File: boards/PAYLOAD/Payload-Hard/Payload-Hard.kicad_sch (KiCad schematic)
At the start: 2 parts

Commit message: LL
LL
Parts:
- added J?: Conn_01x05_Female, symbol Connector:Conn_01x05_Female
- added P?: S3B-PH-SM4-TB, JST_S3B-PH-SM4-TB:JST_S3B-PH-SM4-TB, symbol S3B-PH-SM4-TB:S3B-PH-SM4-TB
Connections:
- net RED: now reaches A.19 (A0)
- net RED: now also J?.3 (Pin_3)
- net NOX: now reaches A.20 (A1)
- net NOX: now also J?.4 (Pin_4)
- net PRE: now reaches A.21 (A2)
- net PRE: now also J?.5 (Pin_5)
- net 5V: now reaches A.27 (+5V)
- net 5V: now also J?.1 (Pin_1), P?.2
- net GND: now reaches A.29 (GND)
- net GND: now also A.4 (GND), J?.2 (Pin_2), P?.1
- net SIG: now reaches A.5 (D2)
- net SIG: now also P?.3
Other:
- moved on the sheet: A, U?
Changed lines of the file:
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@@
 (kicad_sch (version 20211123) (generator eeschema)
   (paper "A4")
-  (symbol (lib_id "Sensor_Gas:3SP_SO2_20") (at 247.65 62.23 0) (unit 1)
-    (in_bom yes) (on_board yes) (fields_autoplaced)
-    (property "Reference" "U?" (id 0) (at 248.7295 59.69 0))
-    (property "Value" "3SP_SO2_20" (id 1) (at 248.7295 62.23 0))
-    (property "Footprint" "" (id 2) (at 247.65 62.23 0)
-      (effects (font (size 1.27 1.27)) hide)
-    )
-    (property "Datasheet" "" (id 3) (at 247.65 62.23 0)
+  (junction (at 163.83 87.63) (diameter 0) (color 0 0 0 0)
+  )
+  (wire (pts (xy 163.83 87.63) (xy 166.37 87.63))
+    (stroke (width 0) (type default) (color 0 0 0 0))
+  )
+  (wire (pts (xy 166.37 87.63) (xy 166.37 86.36))
+    (stroke (width 0) (type default) (color 0 0 0 0))
+  )
+  (wire (pts (xy 163.83 86.36) (xy 163.83 87.63))
+    (stroke (width 0) (type default) (color 0 0 0 0))
+  )
+  (wire (pts (xy 163.83 88.9) (xy 163.83 87.63))
+    (stroke (width 0) (type default) (color 0 0 0 0))
+  )
+  (hierarchical_label "5V" (shape input) (at 232.41 60.96 180)
+    (effects (font (size 1.27 1.27)) (justify right))
+  )
+  (hierarchical_label "NOX" (shape input) (at 176.53 63.5 0)
+    (effects (font (size 1.27 1.27)) (justify left))
+  )
+  (hierarchical_label "PRE" (shape input) (at 163.83 121.92 180)
+    (effects (font (size 1.27 1.27)) (justify right))
+  )
+  (hierarchical_label "SIG" (shape input) (at 151.13 50.8 180)
+    (effects (font (size 1.27 1.27)) (justify right))
+  )
+  (hierarchical_label "NOX" (shape input) (at 163.83 119.38 180)
+    (effects (font (size 1.27 1.27)) (justify right))
+  )
+  (hierarchical_label "RED" (shape input) (at 176.53 60.96 0)
+    (effects (font (size 1.27 1.27)) (justify left))
+  )
+  (hierarchical_label "RED" (shape input) (at 163.83 116.84 180)
+    (effects (font (size 1.27 1.27)) (justify right))
+  )
+  (hierarchical_label "PRE" (shape input) (at 176.53 66.04 0)
+    (effects (font (size 1.27 1.27)) (justify left))
+  )
+  (hierarchical_label "SIG" (shape input) (at 232.41 63.5 180)
+    (effects (font (size 1.27 1.27)) (justify right))
+  )
+  (hierarchical_label "5V" (shape input) (at 168.91 35.56 90)
+    (effects (font (size 1.27 1.27)) (justify left))
+  )
+  (hierarchical_label "5V" (shape input) (at 163.83 111.76 180)
+    (effects (font (size 1.27 1.27)) (justify right))
+  )
+  (symbol (lib_id "power:GND") (at 232.41 58.42 270) (unit 1)
+    (in_bom yes) (on_board yes) (fields_autoplaced)
+    (property "Reference" "#PWR?" (id 0) (at 226.06 58.42 0)
+      (effects (font (size 1.27 1.27)) hide)
+    )
+    (property "Value" "GND" (id 1) (at 228.6 58.4199 90)
+      (effects (font (size 1.27 1.27)) (justify right))
+    )
+    (property "Footprint" "" (id 2) (at 232.41 58.42 0)
+      (effects (font (size 1.27 1.27)) hide)
+    )
+    (property "Datasheet" "" (id 3) (at 232.41 58.42 0)
+      (effects (font (size 1.27 1.27)) hide)
+    )
+    (pin "1")
+  )
+  (symbol (lib_id "Sensor_Gas:3SP_SO2_20") (at 97.79 58.42 0) (unit 1)
+    (in_bom yes) (on_board yes) (fields_autoplaced)
+    (property "Reference" "U?" (id 0) (at 98.8695 55.88 0))
+    (property "Value" "3SP_SO2_20" (id 1) (at 98.8695 58.42 0))
+    (property "Footprint" "" (id 2) (at 97.79 58.42 0)
+      (effects (font (size 1.27 1.27)) hide)
+    )
+    (property "Datasheet" "" (id 3) (at 97.79 58.42 0)
       (effects (font (size 1.27 1.27)) hide)
     )
@@
     (pin "6")
   )
-  (symbol (lib_id "MCU_Module:Arduino_Nano_v3.x") (at 154.94 81.28 0) (unit 1)
-    (in_bom yes) (on_board yes) (fields_autoplaced)
-    (property "Reference" "A" (id 0) (at 159.4994 106.68 0)
-      (effects (font (size 1.27 1.27)) (justify left))
-    )
-    (property "Value" "Arduino_Nano_v3.x" (id 1) (at 159.4994 109.22 0)
-      (effects (font (size 1.27 1.27)) (justify left))
-    )
-    (property "Footprint" "Module:Arduino_Nano" (id 2) (at 154.94 81.28 0)
+  (symbol (lib_id "MCU_Module:Arduino_Nano_v3.x") (at 163.83 60.96 0) (unit 1)
+    (in_bom yes) (on_board yes) (fields_autoplaced)
+    (property "Reference" "A" (id 0) (at 168.3894 86.36 0)
+      (effects (font (size 1.27 1.27)) (justify left))
+    )
+    (property "Value" "Arduino_Nano_v3.x" (id 1) (at 168.3894 88.9 0)
+      (effects (font (size 1.27 1.27)) (justify left))
+    )
+    (property "Footprint" "Module:Arduino_Nano" (id 2) (at 163.83 60.96 0)
       (effects (font (size 1.27 1.27) italic) hide)
     )
-    (property "Datasheet" "http://www.mouser.com/pdfdocs/Gravitech_Arduino_Nano3_0.pdf" (id 3) (at 154.94 81.28 0)
+    (property "Datasheet" "http://www.mouser.com/pdfdocs/Gravitech_Arduino_Nano3_0.pdf" (id 3) (at 163.83 60.96 0)
       (effects (font (size 1.27 1.27)) hide)
     )
@@
     (pin "9")
   )
+  (symbol (lib_id "power:GND") (at 163.83 88.9 0) (unit 1)
+    (in_bom yes) (on_board yes) (fields_autoplaced)
+    (property "Reference" "#PWR?" (id 0) (at 163.83 95.25 0)
+      (effects (font (size 1.27 1.27)) hide)
+    )
+    (property "Value" "GND" (id 1) (at 163.83 93.98 0))
+    (property "Footprint" "" (id 2) (at 163.83 88.9 0)
+      (effects (font (size 1.27 1.27)) hide)
+    )
+    (property "Datasheet" "" (id 3) (at 163.83 88.9 0)
+      (effects (font (size 1.27 1.27)) hide)
+    )
+    (pin "1")
+  )
+  (symbol (lib_id "Connector:Conn_01x05_Female") (at 168.91 116.84 0) (unit 1)
+    (in_bom yes) (on_board yes) (fields_autoplaced)
+    (property "Reference" "J?" (id 0) (at 170.18 115.5699 0)
+      (effects (font (size 1.27 1.27)) (justify left))
+    )
+    (property "Value" "Conn_01x05_Female" (id 1) (at 170.18 118.1099 0)
+      (effects (font (size 1.27 1.27)) (justify left))
+    )
+    (property "Footprint" "" (id 2) (at 168.91 116.84 0)
+      (effects (font (size 1.27 1.27)) hide)
+    )
+    (property "Datasheet" "~" (id 3) (at 168.91 116.84 0)
+      (effects (font (size 1.27 1.27)) hide)
+    )
+    (pin "1")
+    (pin "2")
+    (pin "3")
+    (pin "4")
+    (pin "5")
+  )
+  (symbol (lib_id "S3B-PH-SM4-TB:S3B-PH-SM4-TB") (at 237.49 60.96 0) (unit 1)
+    (in_bom yes) (on_board yes) (fields_autoplaced)
+    (property "Reference" "P?" (id 0) (at 243.84 59.6899 0)
+      (effects (font (size 1.27 1.27)) (justify left))
+    )
+    (property "Value" "S3B-PH-SM4-TB" (id 1) (at 243.84 62.2299 0)
+      (effects (font (size 1.27 1.27)) (justify left))
+    )
+    (property "Footprint" "JST_S3B-PH-SM4-TB:JST_S3B-PH-SM4-TB" (id 2) (at 237.49 60.96 0)
+      (effects (font (size 1.27 1.27)) (justify bottom) hide)
+    )
+    (property "Datasheet" "" (id 3) (at 237.49 60.96 0)
+      (effects (font (size 1.27 1.27)) hide)
+    )
+    (property "MANUFACTURER" "JST" (id 4) (at 237.49 60.96 0)
+      (effects (font (size 1.27 1.27)) (justify bottom) hide)
+    )
+    (pin "1")
+    (pin "2")
+    (pin "3")
+  )
+  (symbol (lib_id "power:GND") (at 163.83 114.3 270) (unit 1)
+    (in_bom yes) (on_board yes)
+    (property "Reference" "#PWR?" (id 0) (at 157.48 114.3 0)
+      (effects (font (size 1.27 1.27)) hide)
+    )
+    (property "Value" "GND" (id 1) (at 160.02 114.3 90)
+      (effects (font (size 1.27 1.27)) (justify right))
+    )
+    (property "Footprint" "" (id 2) (at 163.83 114.3 0)
+      (effects (font (size 1.27 1.27)) hide)
+    )
+    (property "Datasheet" "" (id 3) (at 163.83 114.3 0)
+      (effects (font (size 1.27 1.27)) hide)
+    )
+    (pin "1")
+  )
   (sheet_instances
     (path "/" (page "1"))
   )
   (symbol_instances
+    (path "/196bc3c3-e5ff-458f-8b12-ac7c3d955c8b"
+      (reference "#PWR?") (unit 1) (value "GND") (footprint "")
+    )
+    (path "/b797a9a5-ff96-4bc7-9f7a-f6d641e801e6"
+      (reference "#PWR?") (unit 1) (value "GND") (footprint "")
+    )
+    (path "/e1403e9c-d28d-4e8c-a906-1d3b4236ad77"
+      (reference "#PWR?") (unit 1) (value "GND") (footprint "")
+    )
     (path "/a91a09ae-7da8-46f5-893f-cfe40ca8737a"
       (reference "A") (unit 1) (value "Arduino_Nano_v3.x") (footprint "Module:Arduino_Nano")
     )
+    (path "/bc1d1c15-132d-4a77-beb4-5670c0f8e9de"
+      (reference "J?") (unit 1) (value "Conn_01x05_Female") (footprint "")
+    )
+    (path "/ca60eda0-66cc-44d6-94f2-b6dbdfb5e6f4"
+      (reference "P?") (unit 1) (value "S3B-PH-SM4-TB") (footprint "JST_S3B-PH-SM4-TB:JST_S3B-PH-SM4-TB")
+    )
     (path "/325b982e-7665-4281-8762-9f7b5f3809a1"

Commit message: A Lot
A Lot
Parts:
- added C? (x2): 0.1uF, symbol Device:C
- added C?: 100 nF, Capacitor_SMD:C_0805_2012Metric, symbol D24V50F5:C
- added J?: Micro_SD_Card, Connector_Card:microSD_HC_Hirose_DM3AT-SF-PEJM5, symbol Connector:Micro_SD_Card
- added R? (x5): R_US, symbol Device:R_US
- added R? (x2): 10k, Resistor_SMD:R_0805_2012Metric, symbol D24V50F5:R_US
- added R?: 150 Ohm, symbol Device:R_US
- added U?: Opamp_Dual, symbol Device:Opamp_Dual
- added U?: OPAMP, symbol pspice:OPAMP
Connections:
- net GND: now also C?.1, J?.6 (VSS), J?.9 (SHIELD), R?.2, R?.2, U?.5 (V-)
- net at U?.1 (Working): now also U?.6 (Working)
- net Reference: now reaches U?.4 (Reference)
- net Reference: now also C?.2, U?.2 (-)
- net Counter: now reaches U?.5 (Counter)
- net Counter: now also C?.1, U?.3
- net 3V3: now reaches A.17 (3V3)
- net 3V3: now also C?.2, J?.4 (VDD), R?.1, R?.1, R?.1, R?.1, U?.4 (V+)
- net SO2_Out: now reaches A.22 (A3)
- net SPI_SDCARD_CS: now reaches A.6 (D3)
- net SPI_SDCARD_CS: now also J?.2 (DAT3/CD)
- net SPI_SDCARD_MOSI: now reaches A.7 (D4)
- net SPI_SDCARD_MOSI: now also J?.3 (CMD)
- net SPI_SDCARD_SCK: now reaches A.8 (D5)
- net SPI_SDCARD_SCK: now also J?.5 (CLK)
- net SPI_SDCARD_MISO: now reaches A.9 (D6)
- net SPI_SDCARD_MISO: now also J?.7 (DAT0)
- new net: C?.2, R?.2, U?.1
- new net: C?.1, R?.1, R?.2, U?.2 (-)
- new net: R?.1, R?.2, U?.3 (+)
- new net: R?.1, R?.2, U?.1 (+)
- new net: J?.1 (DAT2), R?.2
- new net: J?.8 (DAT1), R?.2
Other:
- note added: "Arduino V3"
- note added: "CO Sensor"
- note added: "Dust Sensor"
- note added: "Micro_SD_Card_Reader"
- note added: "SO2 Sensor"
- title: (none) -> My Dick is Hard 4 U
- moved on the sheet: U?

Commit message: Schematic Finished
Look it over
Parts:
- added J103: Conn_01x07_Male, symbol Connector:Conn_01x07_Male
- gave numbers to parts that had none: 17
- renumbered A to A101
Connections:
- net 3V3: now also J103.6 (Pin_6)
- net 5V: now also J103.7 (Pin_7)
- net SO2_Out: now also C103.2, R108.2, U103.1
- net SPI_SDCARD_CS: now also J103.2 (Pin_2)
- net SPI_SDCARD_MISO: now also J103.5 (Pin_5)
- net SPI_SDCARD_MOSI: now also J103.3 (Pin_3)
- net SPI_SDCARD_SCK: now also J103.4 (Pin_4)
- net SIG renamed Dust_SIG
- net Dust_SIG: now also J103.1 (Pin_1)
- no-connect marks 0 -> 19
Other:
- note added: "Test Pins"

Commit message: Added SO2 Footprint
See above
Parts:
- C102, C103, R101, R102, R105, R106, R107, R108: footprint (none) -> Resistor_SMD:R_0805_2012Metric
- J102, J103: footprint (none) -> Connector_PinSocket_2.54mm:PinSocket_1x07_P2.54mm_Vertical
- U102: footprint (none) -> Sensor:3SP_SO2_20
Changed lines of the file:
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@@
     (property "Reference" "R101" (id 0) (at 36.195 149.86 90))
     (property "Value" "R_US" (id 1) (at 36.195 152.4 90))
-    (property "Footprint" "" (id 2) (at 36.449 155.194 90)
+    (property "Footprint" "Resistor_SMD:R_0805_2012Metric" (id 2) (at 36.449 155.194 90)
       (effects (font (size 1.27 1.27)) hide)
     )
@@
     (property "Reference" "R108" (id 0) (at 147.32 135.255 90))
     (property "Value" "R_US" (id 1) (at 154.94 135.255 90))
-    (property "Footprint" "" (id 2) (at 150.749 136.779 90)
+    (property "Footprint" "Resistor_SMD:R_0805_2012Metric" (id 2) (at 150.749 136.779 90)
       (effects (font (size 1.27 1.27)) hide)
     )
@@
     (property "Reference" "U102" (id 0) (at 105.9815 150.114 0))
     (property "Value" "3SP_SO2_20" (id 1) (at 105.9815 152.654 0))
-    (property "Footprint" "" (id 2) (at 104.902 152.654 0)
+    (property "Footprint" "Sensor:3SP_SO2_20" (id 2) (at 104.902 152.654 0)
       (effects (font (size 1.27 1.27)) hide)
     )
@@
       (effects (font (size 1.27 1.27)) (justify left))
     )
-    (property "Footprint" "" (id 2) (at 81.6102 151.765 0)
+    (property "Footprint" "Resistor_SMD:R_0805_2012Metric" (id 2) (at 81.6102 151.765 0)
       (effects (font (size 1.27 1.27)) hide)
     )
@@
     (property "Reference" "J103" (id 0) (at 237.617 90.17 0))
     (property "Value" "Conn_01x07_Male" (id 1) (at 237.617 92.71 0))
-    (property "Footprint" "" (id 2) (at 236.982 102.616 0)
+    (property "Footprint" "Connector_PinSocket_2.54mm:PinSocket_1x07_P2.54mm_Vertical" (id 2) (at 236.982 102.616 0)
       (effects (font (size 1.27 1.27)) hide)
     )
@@
     (property "Reference" "R106" (id 0) (at 133.985 142.24 90))
     (property "Value" "150 Ohm" (id 1) (at 133.985 147.32 90))
-    (property "Footprint" "" (id 2) (at 134.239 143.764 90)
+    (property "Footprint" "Resistor_SMD:R_0805_2012Metric" (id 2) (at 134.239 143.764 90)
       (effects (font (size 1.27 1.27)) hide)
     )
@@
       (effects (font (size 1.27 1.27)) (justify left))
     )
-    (property "Footprint" "" (id 2) (at 44.831 164.084 90)
+    (property "Footprint" "Resistor_SMD:R_0805_2012Metric" (id 2) (at 44.831 164.084 90)
       (effects (font (size 1.27 1.27)) hide)
     )
@@
       (effects (font (size 1.27 1.27)) (justify left))
     )
-    (property "Footprint" "" (id 2) (at 137.541 164.084 90)
+    (property "Footprint" "Resistor_SMD:R_0805_2012Metric" (id 2) (at 137.541 164.084 90)
       (effects (font (size 1.27 1.27)) hide)
     )
@@
     (property "Reference" "C103" (id 0) (at 147.955 142.24 90))
     (property "Value" "0.1uF" (id 1) (at 153.035 142.24 90))
-    (property "Footprint" "" (id 2) (at 154.305 143.8148 0)
+    (property "Footprint" "Resistor_SMD:R_0805_2012Metric" (id 2) (at 154.305 143.8148 0)
       (effects (font (size 1.27 1.27)) hide)
     )
@@
       (effects (font (size 1.27 1.27)) (justify left))
     )
-    (property "Footprint" "" (id 2) (at 168.91 116.84 0)
+    (property "Footprint" "Connector_PinSocket_2.54mm:PinSocket_1x07_P2.54mm_Vertical" (id 2) (at 168.91 116.84 0)
       (effects (font (size 1.27 1.27)) hide)
     )
@@
     (property "Reference" "R105" (id 0) (at 129.54 149.225 90))
     (property "Value" "R_US" (id 1) (at 129.54 154.305 90))
-    (property "Footprint" "" (id 2) (at 129.794 150.749 90)
+    (property "Footprint" "Resistor_SMD:R_0805_2012Metric" (id 2) (at 129.794 150.749 90)
       (effects (font (size 1.27 1.27)) hide)
     )
@@
     )
     (path "/3785a743-d774-4bea-ab16-8819dd3926f7"
-      (reference "C102") (unit 1) (value "0.1uF") (footprint "")
+      (reference "C102") (unit 1) (value "0.1uF") (footprint "Resistor_SMD:R_0805_2012Metric")
     )
     (path "/ba5b7d76-cf69-4698-9e2c-a9beaffc4bab"
-      (reference "C103") (unit 1) (value "0.1uF") (footprint "")
+      (reference "C103") (unit 1) (value "0.1uF") (footprint "Resistor_SMD:R_0805_2012Metric")
     )
     (path "/aad04261-e627-4861-b410-22b45606c5aa"
@@
     )
     (path "/bc1d1c15-132d-4a77-beb4-5670c0f8e9de"
-      (reference "J102") (unit 1) (value "Conn_01x05_Female") (footprint "")
+      (reference "J102") (unit 1) (value "Conn_01x05_Female") (footprint "Connector_PinSocket_2.54mm:PinSocket_1x07_P2.54mm_Vertical")
     )
     (path "/3fd118c7-9e7a-4c5d-a6a1-1ac96967b8b9"
-      (reference "J103") (unit 1) (value "Conn_01x07_Male") (footprint "")
+      (reference "J103") (unit 1) (value "Conn_01x07_Male") (footprint "Connector_PinSocket_2.54mm:PinSocket_1x07_P2.54mm_Vertical")
     )
     (path "/ca60eda0-66cc-44d6-94f2-b6dbdfb5e6f4"
@@
     )
     (path "/193d0700-60b7-4689-978d-a547e5d96307"
-      (reference "R101") (unit 1) (value "R_US") (footprint "")
+      (reference "R101") (unit 1) (value "R_US") (footprint "Resistor_SMD:R_0805_2012Metric")
     )
     (path "/9250d66a-a257-4378-b8f5-d3bb8f4fd8a7"
-      (reference "R102") (unit 1) (value "R_US") (footprint "")
+      (reference "R102") (unit 1) (value "R_US") (footprint "Resistor_SMD:R_0805_2012Metric")
     )
     (path "/7d9c8643-fe41-4ec3-bc8b-c5590f819487"
@@
     )
     (path "/c6a3b258-40e8-4601-9207-4a2518b36ffa"
-      (reference "R105") (unit 1) (value "R_US") (footprint "")
+      (reference "R105") (unit 1) (value "R_US") (footprint "Resistor_SMD:R_0805_2012Metric")
     )
     (path "/85f2d637-1216-4a5c-bbc8-0ce2cc90f2ed"
-      (reference "R106") (unit 1) (value "150 Ohm") (footprint "")
+      (reference "R106") (unit 1) (value "150 Ohm") (footprint "Resistor_SMD:R_0805_2012Metric")
     )
     (path "/b9e4634e-89c4-4a0f-b5cd-8f409b547f37"
-      (reference "R107") (unit 1) (value "R_US") (footprint "")
+      (reference "R107") (unit 1) (value "R_US") (footprint "Resistor_SMD:R_0805_2012Metric")
     )
     (path "/2a4fc409-e0b4-4d3d-9f51-9b6d5ca0ec54"
-      (reference "R108") (unit 1) (value "R_US") (footprint "")
+      (reference "R108") (unit 1) (value "R_US") (footprint "Resistor_SMD:R_0805_2012Metric")
     )
     (path "/dea62b05-f679-4afa-8d03-361e4a7b827c"
@@
     )
     (path "/325b982e-7665-4281-8762-9f7b5f3809a1"
-      (reference "U102") (unit 1) (value "3SP_SO2_20") (footprint "")
+      (reference "U102") (unit 1) (value "3SP_SO2_20") (footprint "Sensor:3SP_SO2_20")
     )
     (path "/03c3a716-241d-43da-b0af-01f857d80378"

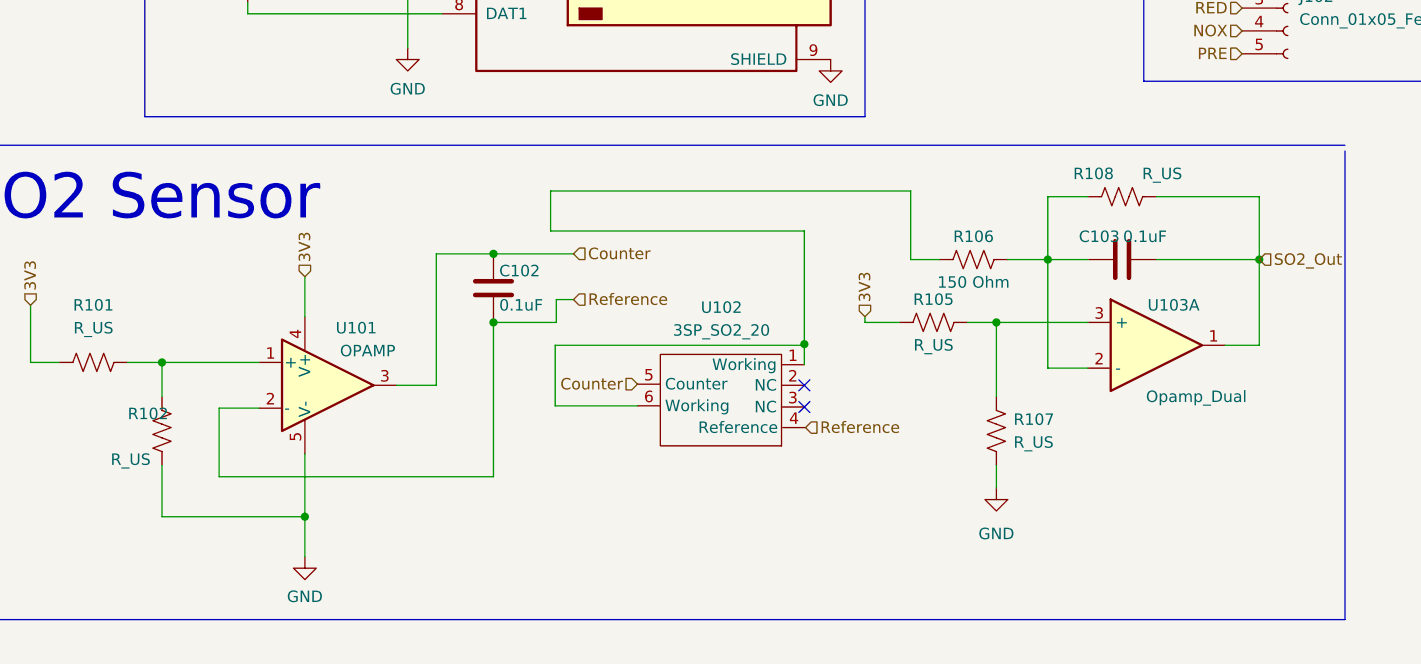
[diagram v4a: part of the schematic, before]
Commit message: Fixed Op Amp Circuitry
Fixed Op Amp Circuitry
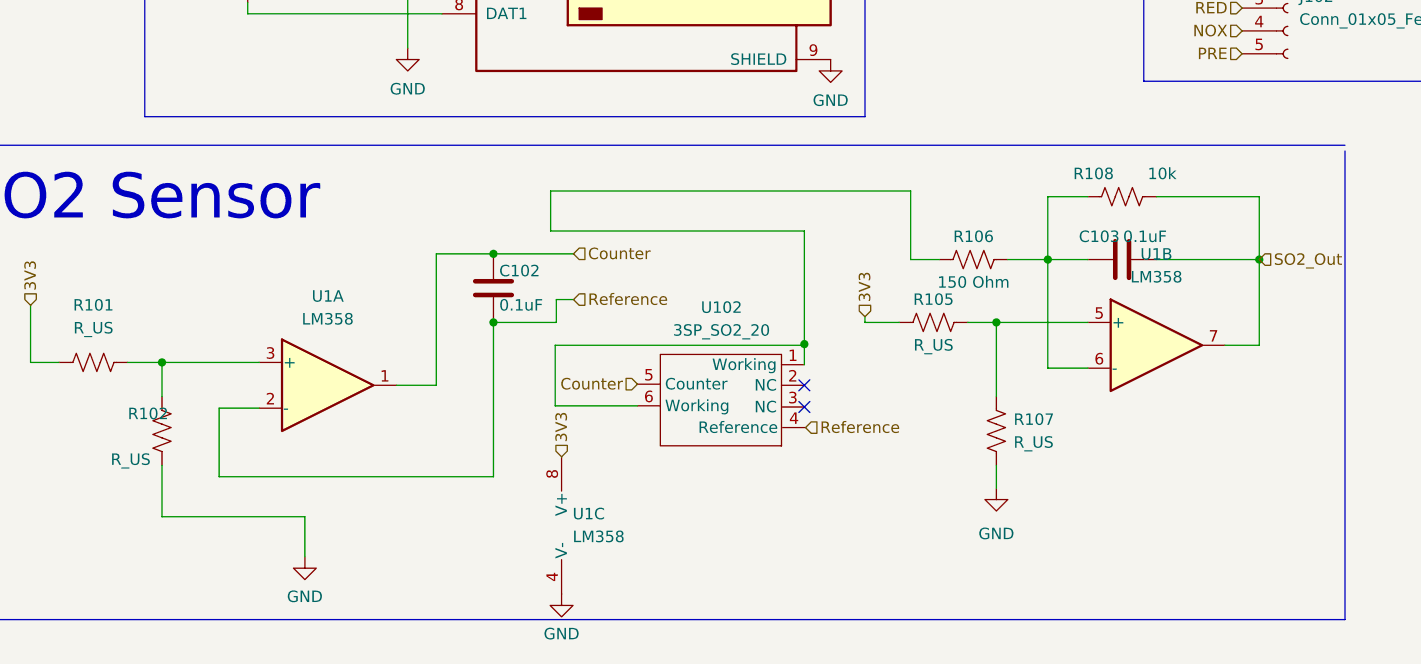
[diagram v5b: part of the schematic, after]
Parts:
- removed U101: OPAMP, symbol pspice:OPAMP
- removed U103: Opamp_Dual, symbol Device:Opamp_Dual
- added U1: LM358, Package_DIP:DIP-8_W10.16mm, symbol Amplifier_Operational:LM358
- J102: footprint Connector_PinSocket_2.54mm:PinSocket_1x07_P2.54mm_Vertical -> Connector_PinSocket_2.54mm:PinSocket_1x05_P2.54mm_Vertical
- R108: value R_US -> 10k
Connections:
- net 3V3: now also U1.8 (V+)
- net Counter: now also U1.1
- net GND: now also U1.4 (V-)
- net Reference: now also U1.2 (-)
- net SO2_Out: now also U1.7
- net at C103.1, R106.2, R108.1: now also U1.6 (-)
- net at R105.2, R107.1: now also U1.5 (+)
- net at R101.2, R102.1: now also U1.3 (+)
